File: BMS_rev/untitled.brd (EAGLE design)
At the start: 122.5 x 87.5 mm, 26 parts, among them J1 U.FL-R-SMT(01), U1 ESP32-DEVKITC-32D, U2 PCF8574AT

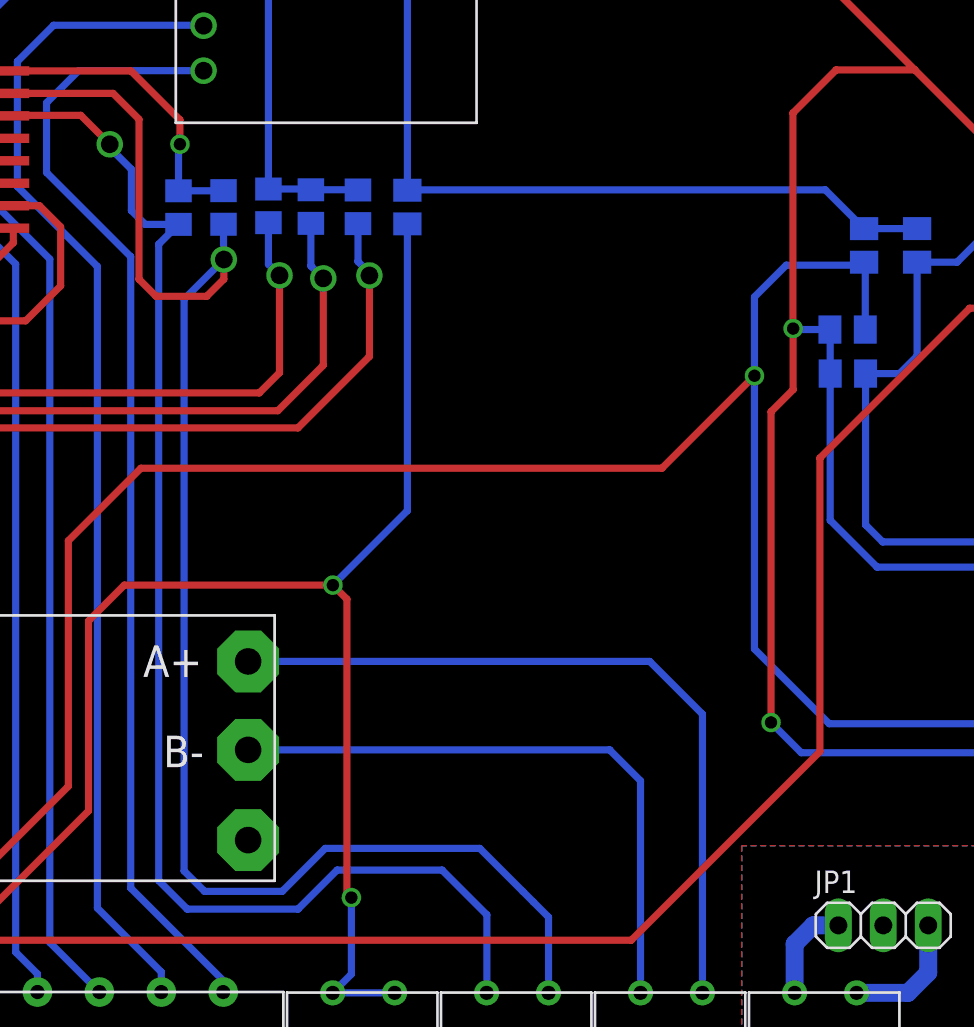
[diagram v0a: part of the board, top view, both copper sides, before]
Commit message: menambahkan pullup i2c
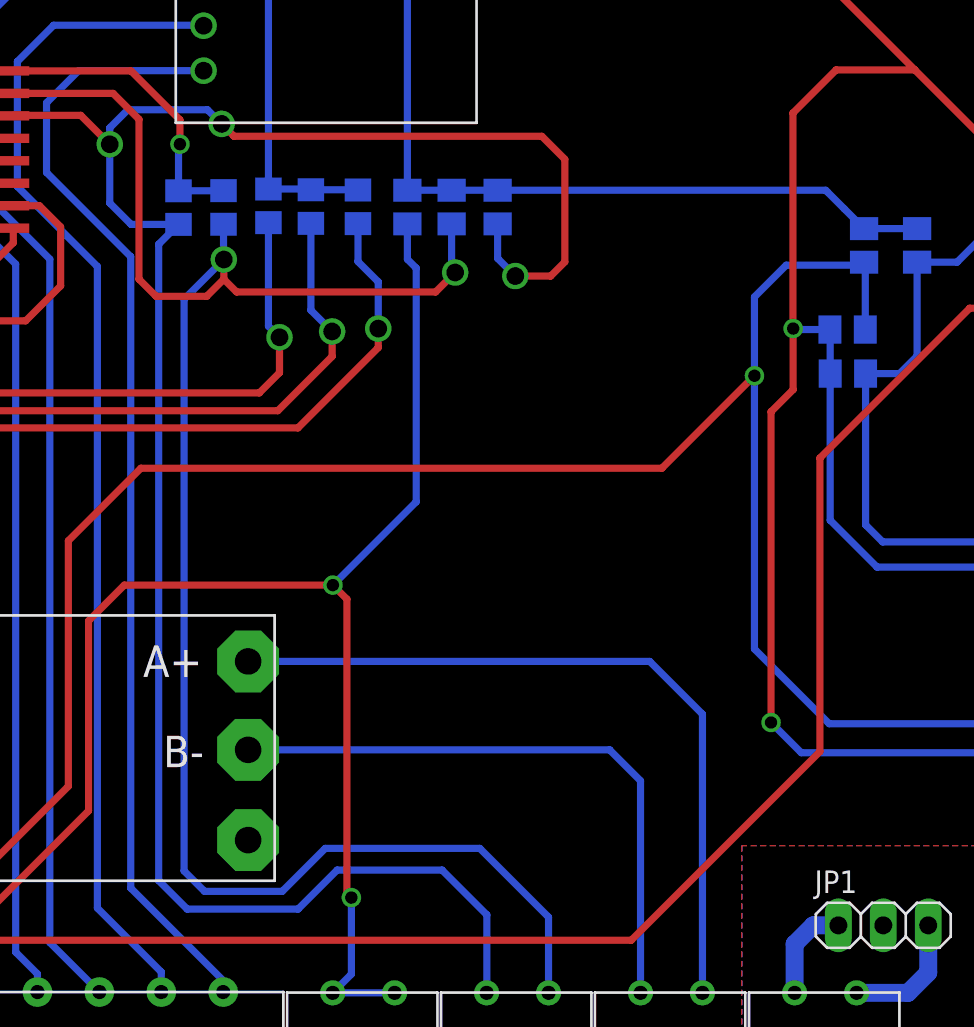
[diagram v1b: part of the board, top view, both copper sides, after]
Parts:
- added R2, R3: (no value), adafruit:M0805
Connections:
- net 3V3: now also R2.2, R3.2
- net SCL: now also R3.1
- net SDA: now also R2.1
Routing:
- net SCL: track 139.4 -> 180.4 mm, vias 2 -> 4
- net SDA: track 140.5 -> 157.2 mm, vias 2 -> 3

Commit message: PCB BMS
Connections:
- removed net VCC: R28.2, R29.1, U2.16
- net OUT+: now also R28.2, R29.1, U2.16
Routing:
- net OUT+: track 179.2 -> 269.5 mm, vias 1 -> 2
- net VCC: track 17.2 -> 0.00 mm, vias 1 -> 0
- net RST: track 190.7 -> 188.9 mm
- net GND: track 392.9 -> 394.7 mm
